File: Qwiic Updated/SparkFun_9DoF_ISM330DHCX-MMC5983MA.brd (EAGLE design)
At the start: 25.4 x 25.4 mm, 59 parts, among them J1 QWIIC_RIGHT_ANGLE, J2 QWIIC_RIGHT_ANGLE, U1 ISM330DHCX, U2 MMC5983MA_QFN16

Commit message: More updates to the routing
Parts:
- moved R6 0.54 mm to (19.7, 6.99)
- moved 6DOF_ADDR 0.38 mm to (19.8, 8.00)
- moved R5 0.38 mm to (19.7, 9.02)
- moved I2C_PU 0.06 mm to (12.9, 8.15), turned to 0 degrees
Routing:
- net 3.3V: track 0.00 -> 32.8 mm, vias 0 -> 5
- net ISM_INT2: track 0.00 -> 15.5 mm, vias 0 -> 2
- net N$5: track 0.00 -> 4.62 mm, vias 0 -> 1
- net N$7: track 0.00 -> 3.13 mm, vias 0 -> 1
- net N$1: track 0.00 -> 3.08 mm, vias 0 -> 1
- net N$6: track 0.00 -> 2.83 mm, vias 0 -> 1
- net POCI/SA0: track 35.7 -> 33.5 mm
- net GND: vias 6 -> 10

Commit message: Finishes routing
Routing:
- net 3.3V: track 32.8 -> 60.2 mm, vias 5 -> 6
- net N$3: track 0.00 -> 2.35 mm, vias 0 -> 1
- net N$2: track 0.00 -> 1.63 mm
- net SCL/SCK: track 50.3 -> 51.7 mm
- net GND: vias 10 -> 23

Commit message: Vias applied
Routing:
- net 3.3V: track 60.2 -> 59.1 mm
- net GND: vias 23 -> 31
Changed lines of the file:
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@@
 <setting verticaltext="up"/>
 </settings>
-<grid distance="0.05" unitdist="inch" unit="inch" style="dots" multiple="1" display="yes" altdistance="0.005" altunitdist="inch" altunit="inch"/>
+<grid distance="0.05" unitdist="inch" unit="inch" style="dots" multiple="1" display="yes" altdistance="0.001" altunitdist="inch" altunit="inch"/>
 <layers>
 <layer number="1" name="Top" color="4" fill="1" visible="yes" active="yes"/>
@@
 <via x="10.668" y="3.683" extent="1-16" drill="0.3048"/>
 <via x="9.652" y="7.112" extent="1-16" drill="0.3048"/>
-<via x="17.145" y="6.223" extent="1-16" drill="0.3048"/>
+<via x="17.0942" y="7.3406" extent="1-16" drill="0.3048"/>
 <via x="8.001" y="6.223" extent="1-16" drill="0.3048"/>
 <via x="5.334" y="6.604" extent="1-16" drill="0.3048"/>
 <via x="5.715" y="9.779" extent="1-16" drill="0.3048"/>
 <via x="3.302" y="8.255" extent="1-16" drill="0.3048"/>
+<via x="18.161" y="16.002" extent="1-16" drill="0.3048"/>
+<via x="15.8242" y="17.0942" extent="1-16" drill="0.3048"/>
+<via x="17.145" y="8.6868" extent="1-16" drill="0.3048"/>
+<via x="14.8336" y="8.4328" extent="1-16" drill="0.3048"/>
+<via x="10.9728" y="5.715" extent="1-16" drill="0.3048"/>
+<via x="14.8844" y="6.1722" extent="1-16" drill="0.3048"/>
+<via x="15.8242" y="19.8882" extent="1-16" drill="0.3048"/>
+<via x="15.8242" y="18.2626" extent="1-16" drill="0.3048"/>
 </signal>
 <signal name="SCL/SCK">
@@
 <wire x1="16.51" y1="8.89" x2="17.653" y2="10.033" width="0.2032" layer="1"/>
 <wire x1="17.653" y1="10.033" x2="21.59" y2="10.033" width="0.2032" layer="1"/>
-<wire x1="13.454" y1="18.389" x2="13.454" y2="18.788" width="0.2032" layer="1"/>
-<wire x1="13.454" y1="18.788" x2="13.716" y2="19.05" width="0.2032" layer="1"/>
-<wire x1="13.716" y1="19.05" x2="18.119975" y2="19.05" width="0.2032" layer="1"/>
+<wire x1="13.454" y1="18.389" x2="13.454" y2="18.8642" width="0.2032" layer="1"/>
+<wire x1="13.454" y1="18.8642" x2="13.6398" y2="19.05" width="0.2032" layer="1"/>
+<wire x1="13.6398" y1="19.05" x2="18.119975" y2="19.05" width="0.2032" layer="1"/>
 <wire x1="13.97" y1="1.27" x2="12.104" y2="3.136" width="0.2032" layer="1"/>
 <wire x1="12.104" y1="3.136" x2="12.104" y2="5.37845" width="0.2032" layer="1"/>
@@
 <wire x1="14.3705" y1="10.656" x2="16.383" y2="12.6685" width="0.2032" layer="1"/>
 <wire x1="13.8625" y1="10.656" x2="14.3705" y2="10.656" width="0.2032" layer="1"/>
-<via x="16.383" y="17.018" extent="1-16" drill="0.35"/>
-<wire x1="16.383" y1="17.018" x2="16.383" y2="20.574" width="0.2032" layer="16"/>
+<via x="16.637" y="17.0942" extent="1-16" drill="0.35"/>
+<wire x1="16.637" y1="17.0942" x2="16.637" y2="20.32" width="0.2032" layer="16"/>
 <wire x1="15.113" y1="21.844" x2="8.636" y2="21.844" width="0.2032" layer="16"/>
 <wire x1="8.636" y1="21.844" x2="6.35" y2="24.13" width="0.2032" layer="16"/>
-<wire x1="16.383" y1="12.6685" x2="16.383" y2="17.018" width="0.2032" layer="1"/>
-<wire x1="16.383" y1="20.574" x2="15.113" y2="21.844" width="0.2032" layer="16"/>
+<wire x1="16.383" y1="12.6685" x2="16.383" y2="16.51" width="0.2032" layer="1"/>
+<wire x1="16.637" y1="17.0942" x2="16.637" y2="16.764" width="0.2032" layer="1"/>
+<wire x1="16.383" y1="16.51" x2="16.637" y2="16.764" width="0.2032" layer="1"/>
+<wire x1="16.637" y1="20.32" x2="15.113" y2="21.844" width="0.2032" layer="16"/>
 </signal>
 <signal name="3.3V">
@@
 <wire x1="13.464" y1="16.127" x2="12.954" y2="16.637" width="0.2032" layer="1"/>
 <wire x1="12.954" y1="16.637" x2="12.954" y2="18.389" width="0.2032" layer="1"/>
-<wire x1="12.954" y1="18.389" x2="12.954" y2="19.47" width="0.2032" layer="1"/>
 <wire x1="12.954" y1="19.47" x2="13.296" y2="19.812" width="0.2032" layer="1"/>
 <wire x1="8.89" y1="1.27" x2="8.89" y2="5.969" width="0.4064" layer="16"/>
@@
 <wire x1="10.414" y1="6.35" x2="12.573" y2="6.35" width="0.4064" layer="16"/>
 <wire x1="12.573" y1="6.35" x2="12.6365" y2="6.4135" width="0.4064" layer="16"/>
+<polygon width="0.0508" layer="1" thermals="no">
+<vertex x="12.827" y="18.3388"/>
+<vertex x="12.827" y="18.923"/>
+<vertex x="12.7508" y="18.9992"/>
+<vertex x="12.7508" y="20.32"/>
+<vertex x="13.843" y="20.32"/>
+<vertex x="13.843" y="19.2786"/>
+<vertex x="13.462" y="19.2786"/>
+<vertex x="13.1064" y="18.923"/>
+<vertex x="13.1064" y="18.3388"/>
+</polygon>
 </signal>
 <signal name="N$5">
@@
 <contactref element="6DOF_ADDR" pad="3"/>
 <contactref element="R5" pad="1"/>
-<wire x1="18.8604" y1="9.017" x2="17.863425" y2="9.017" width="0.2032" layer="1"/>
-<wire x1="17.863425" y1="9.017" x2="17.8217125" y2="9.0587125" width="0.2032" layer="1"/>
-<via x="17.8217125" y="9.0587125" extent="1-16" drill="0.3048"/>
-<wire x1="17.8217125" y1="9.0587125" x2="17.838025" y2="9.0424" width="0.2032" layer="16"/>
-<wire x1="17.838025" y1="9.0424" x2="19.84375" y2="9.0424" width="0.2032" layer="16"/>
+<wire x1="18.8604" y1="9.017" x2="17.914225" y2="9.017" width="0.2032" layer="1"/>
+<wire x1="17.914225" y1="9.017" x2="17.8979125" y2="9.0333125" width="0.2032" layer="1"/>
+<via x="17.8979125" y="9.0333125" extent="1-16" drill="0.3048"/>
+<wire x1="17.8979125" y1="9.0333125" x2="17.907" y2="9.0424" width="0.2032" layer="16"/>
+<wire x1="17.907" y1="9.0424" x2="19.84375" y2="9.0424" width="0.2032" layer="16"/>
 </signal>
 <signal name="N$7">
 <contactref element="R6" pad="2"/>
 <contactref element="6DOF_ADDR" pad="1"/>
-<wire x1="19.84375" y1="6.9596" x2="17.8054" y2="6.9596" width="0.2032" layer="16"/>
-<wire x1="17.8054" y1="6.9596" x2="17.78" y2="6.985" width="0.2032" layer="16"/>
-<via x="17.78" y="6.985" extent="1-16" drill="0.3048"/>
-<wire x1="18.835" y1="6.985" x2="17.78" y2="6.985" width="0.2032" layer="1"/>
+<wire x1="19.84375" y1="6.9596" x2="17.8816" y2="6.9596" width="0.2032" layer="16"/>
+<via x="17.8816" y="6.9596" extent="1-16" drill="0.3048"/>
+<wire x1="18.835" y1="6.985" x2="18.8096" y2="6.9596" width="0.2032" layer="1"/>
+<wire x1="18.8096" y1="6.9596" x2="17.8816" y2="6.9596" width="0.2032" layer="1"/>
 </signal>
 <signal name="SDA/PICO">
@@
 <contactref element="U2" pad="15"/>
 <contactref element="JP3" pad="3"/>
-<wire x1="14.196" y1="17.127" x2="15.0824" y2="17.127" width="0.2032" layer="1"/>
-<wire x1="15.0824" y1="17.127" x2="15.113" y2="17.0964" width="0.2032" layer="1"/>
-<via x="15.113" y="17.0964" extent="1-16" drill="0.35"/>
-<wire x1="15.113" y1="17.0964" x2="15.113" y2="19.939" width="0.2032" layer="16"/>
-<wire x1="15.113" y1="19.939" x2="14.351" y2="20.701" width="0.2032" layer="16"/>
+<wire x1="14.196" y1="17.127" x2="15.0316" y2="17.127" width="0.2032" layer="1"/>
+<wire x1="15.0316" y1="17.127" x2="15.0622" y2="17.0964" width="0.2032" layer="1"/>
+<via x="15.0622" y="17.0964" extent="1-16" drill="0.35"/>
+<wire x1="15.0622" y1="17.0964" x2="15.0622" y2="19.9898" width="0.2032" layer="16"/>
+<wire x1="15.0622" y1="19.9898" x2="14.351" y2="20.701" width="0.2032" layer="16"/>
 <wire x1="14.351" y1="20.701" x2="11.557" y2="20.701" width="0.2032" layer="16"/>
 <wire x1="11.557" y1="20.701" x2="11.43" y2="20.828" width="0.2032" layer="16"/>

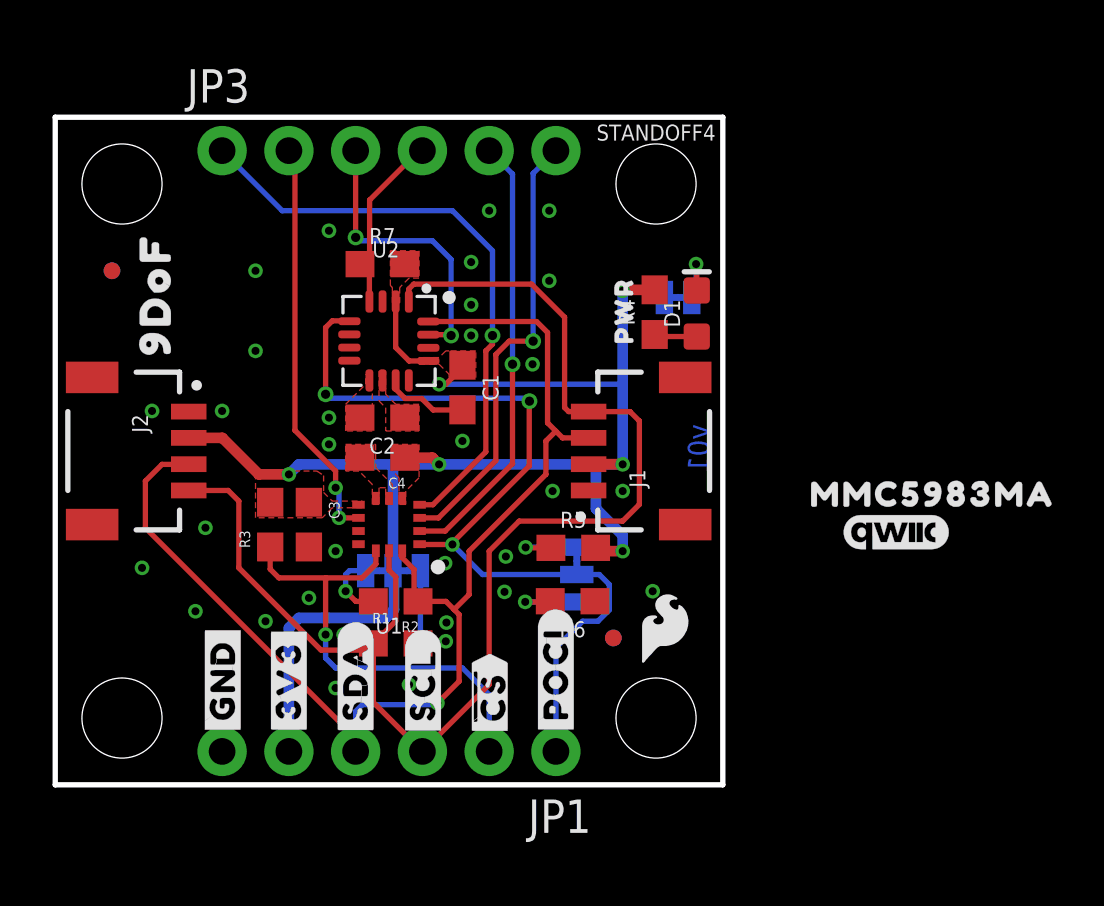
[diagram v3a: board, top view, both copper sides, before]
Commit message: Adds text to schematic, adds jumpers to SDX and SCX
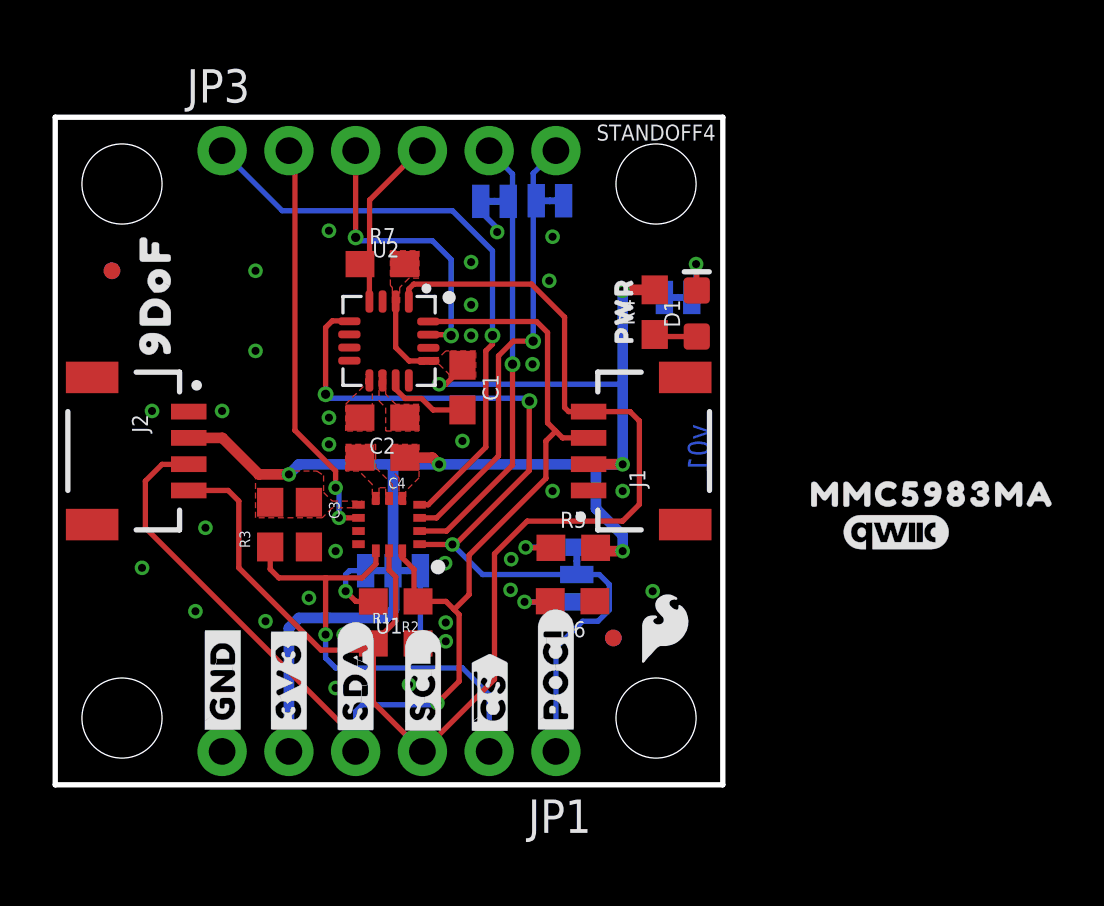
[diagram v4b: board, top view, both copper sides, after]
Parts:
- added SCX, SDX: JUMPER-SMT_2_NC_TRACE_SILK, SparkFun-Jumpers:SMT-JUMPER_2_NC_TRACE_SILK
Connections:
- net GND: now also SCX.1, SDX.1
- net SCX: now also SCX.2
- net SDX: now also SDX.2
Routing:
- net GND: track 3.20 -> 4.63 mm

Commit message: Adds silk
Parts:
- added U$10: (no value), top:#INT1#2
- added U$11: (no value), top:#INT2#2
- added U$12: (no value), top:#MINT#4
- added U$19: (no value), top:##MCS##5
- added U$20: (no value), top:#SDX#7
- added U$23: (no value), top:#SCX#8
- added U$31: (no value), top:MINT3
- added U$34: (no value), top:#MCS#6
- added U$35: (no value), top:#SDX#9
- added U$36: (no value), top:#SCX#11
- added U$39: (no value), top:##ACS##8
- added U$7: (no value), ISMTop:ISM330DHCX331
- added U$8: (no value), top:#INT1#0
- added U$9: (no value), top:#INT2#3
- U$27: device bot:##CS##8 -> top:##ACS##6
- U$3: device top:##CS##7 -> ISMTop:ISM330DHCX331
- U$4: device top:#SDA#4 -> top:SDA14
- U$5: device top:#SCL#5 -> top:SCL13
- moved LOGO1 30.7 mm to (2.29, 17.2)
- moved U$21 28.8 mm to (4.95, 6.60)
- moved U$24 13.5 mm to (2.54, 5.21), turned to 0 degrees
- moved U$3 12.3 mm to (5.08, 7.87), turned to 0 degrees
- moved U$27 0.58 mm to (16.5, 3.94)
- moved U$4 0.53 mm to (10.9, 3.81)
- moved U$6 0.51 mm to (18.5, 4.22)
- moved U$33 0.43 mm to (22.6, 7.24)
- moved U$40 0.41 mm to (22.5, 8.89)
- moved SCX 0.38 mm to (19.2, 22.2)
- moved SDX 0.25 mm to (16.5, 22.2)
- moved R6 0.20 mm to (19.7, 7.19)
- moved U$5 0.16 mm to (14.1, 3.68)

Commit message: Adds a via
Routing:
- net GND: vias 31 -> 32
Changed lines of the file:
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@@
 <wire x1="16.8148" y1="20.9296" x2="15.9385" y2="21.8059" width="0.2032" layer="16"/>
 <wire x1="15.9385" y1="21.8059" x2="15.9385" y2="22.1996" width="0.2032" layer="16"/>
+<via x="16.0528" y="6.6548" extent="1-16" drill="0.3048"/>
 </signal>
 <signal name="SCL/SCK">
